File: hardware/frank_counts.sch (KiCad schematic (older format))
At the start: 20 parts, among them U1 MCP23017_SP

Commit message: Wire up all components
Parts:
- added J1: Trigger, symbol Connector:AudioJack2
- added J2: V/OCT, symbol Connector:AudioJack2
- added R?: 7.7k, symbol Device:R
- added R? (x2): 10k, symbol Device:R
- added RV? (x8): R_POT, symbol Device:R_POT
- added SW1: Shift, symbol Switch:SW_Push
- added U?: MCP3008, symbol Analog_ADC:MCP3008
- added U?: MCP4822, symbol Analog_DAC:MCP4822
- added U? (x2): LM324, symbol Amplifier_Operational:LM324
- renumbered A1 to A?, D1 to D?, D2 to D?, D3 to D?, D4 to D?, D5 to D?, D6 to D?, D7 to D?, D8 to D?, R1 to R?, R2 to R?, R3 to R?, R4 to R?, R5 to R?, R6 to R?, R7 to R?, R8 to R?, R9 to R?, R10 to R?, U1 to U?
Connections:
- net labels added: +12V
- wire segments 71 -> 174
- no-connect marks 10 -> 11
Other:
- note added: "Don’t forget power stabilising CAPS!!"
- moved on the sheet: R?

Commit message: Name some resistors
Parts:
- gave numbers to parts that had none: 12
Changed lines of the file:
@@
 Connection ~ 3050 800
 $Comp
-L Device:R R?
+L Device:R R2
 U 1 1 5EB1EFDE
 P 3500 1000
-F 0 "R?" H 3570 1046 50  0000 L CNN
+F 0 "R2" H 3570 1046 50  0000 L CNN
 F 1 "1k" H 3570 955 50  0000 L CNN
 F 2 "" V 3430 1000 50  0001 C CNN
@@
 $EndComp
 $Comp
-L Device:R R?
+L Device:R R3
 U 1 1 5EB24FDB
 P 6600 2200
-F 0 "R?" V 6393 2200 50  0000 C CNN
+F 0 "R3" V 6393 2200 50  0000 C CNN
 F 1 "200" V 6484 2200 50  0000 C CNN
 F 2 "" V 6530 2200 50  0001 C CNN
@@
 $EndComp
 $Comp
-L Device:R R?
+L Device:R R4
 U 1 1 5EB2606A
 P 7150 2200
-F 0 "R?" V 6943 2200 50  0000 C CNN
+F 0 "R4" V 6943 2200 50  0000 C CNN
 F 1 "200" V 7034 2200 50  0000 C CNN
 F 2 "" V 7080 2200 50  0001 C CNN
@@
 $EndComp
 $Comp
-L Device:R R?
+L Device:R R5
 U 1 1 5EB26460
 P 7700 2200
-F 0 "R?" V 7493 2200 50  0000 C CNN
+F 0 "R5" V 7493 2200 50  0000 C CNN
 F 1 "200" V 7584 2200 50  0000 C CNN
 F 2 "" V 7630 2200 50  0001 C CNN
@@
 $EndComp
 $Comp
-L Device:R R?
+L Device:R R6
 U 1 1 5EB268FE
 P 8250 2200
-F 0 "R?" V 8043 2200 50  0000 C CNN
+F 0 "R6" V 8043 2200 50  0000 C CNN
 F 1 "200" V 8134 2200 50  0000 C CNN
 F 2 "" V 8180 2200 50  0001 C CNN
@@
 $EndComp
 $Comp
-L Device:R R?
+L Device:R R7
 U 1 1 5EB26BCE
 P 8800 2200
-F 0 "R?" V 8593 2200 50  0000 C CNN
+F 0 "R7" V 8593 2200 50  0000 C CNN
 F 1 "200" V 8684 2200 50  0000 C CNN
 F 2 "" V 8730 2200 50  0001 C CNN
@@
 $EndComp
 $Comp
-L Device:R R?
+L Device:R R8
 U 1 1 5EB270AB
 P 9350 2200
-F 0 "R?" V 9143 2200 50  0000 C CNN
+F 0 "R8" V 9143 2200 50  0000 C CNN
 F 1 "200" V 9234 2200 50  0000 C CNN
 F 2 "" V 9280 2200 50  0001 C CNN
@@
 $EndComp
 $Comp
-L Device:R R?
+L Device:R R9
 U 1 1 5EB2750A
 P 9900 2200
-F 0 "R?" V 9693 2200 50  0000 C CNN
+F 0 "R9" V 9693 2200 50  0000 C CNN
 F 1 "200" V 9784 2200 50  0000 C CNN
 F 2 "" V 9830 2200 50  0001 C CNN
@@
 $EndComp
 $Comp
-L Device:R R?
+L Device:R R10
 U 1 1 5EB27EEC
 P 10450 2200
-F 0 "R?" V 10243 2200 50  0000 C CNN
+F 0 "R10" V 10243 2200 50  0000 C CNN
 F 1 "200" V 10334 2200 50  0000 C CNN
 F 2 "" V 10380 2200 50  0001 C CNN
@@
 	5300 5450 6800 5450
 $Comp
-L Device:R R?
+L Device:R R12
 U 1 1 5EEC68B4
 P 7150 6250
-F 0 "R?" V 6943 6250 50  0000 C CNN
+F 0 "R12" V 6943 6250 50  0000 C CNN
 F 1 "7.7k" V 7034 6250 50  0000 C CNN
 F 2 "" V 7080 6250 50  0001 C CNN
@@
 	7000 5050 7000 5250
 $Comp
-L Device:R R?
+L Device:R R11
 U 1 1 5EF2D5A3
 P 6200 6250
-F 0 "R?" V 5993 6250 50  0000 C CNN
+F 0 "R11" V 5993 6250 50  0000 C CNN
 F 1 "10k" V 6084 6250 50  0000 C CNN
 F 2 "" V 6130 6250 50  0001 C CNN
@@
 	1250 1650 1300 1650
 $Comp
-L Device:R R?
+L Device:R R1
 U 1 1 5F110ED0
 P 1300 1900
-F 0 "R?" V 1093 1900 50  0000 C CNN
+F 0 "R1" V 1093 1900 50  0000 C CNN
 F 1 "10k" V 1184 1900 50  0000 C CNN
 F 2 "" V 1230 1900 50  0001 C CNN

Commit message: Start v2 of schematic, using STM32
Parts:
- removed A?: Arduino_UNO_R3, Module:Arduino_UNO_R3, symbol MCU_Module:Arduino_UNO_R3
- removed D? (x8): LED, symbol Device:LED
- removed J1: Trigger, symbol Connector:AudioJack2
- removed J2: V/OCT, symbol Connector:AudioJack2
- removed R1, R11: 10k, symbol Device:R
- removed R10, R3, R4, R5, R6, R7, R8, R9: 200, symbol Device:R
- removed R12: 7.7k, symbol Device:R
- removed R2, R?: 1k, symbol Device:R
- removed RV? (x8): R_POT, symbol Device:R_POT
- removed SW1: Shift, symbol Switch:SW_Push
- removed U?: MCP23017_SP, Package_DIP:DIP-28_W7.62mm, symbol Interface_Expansion:MCP23017_SP
- removed U?: MCP3008, symbol Analog_ADC:MCP3008
- removed U?: MCP4822, symbol Analog_DAC:MCP4822
- removed U? (x2): LM324, symbol Amplifier_Operational:LM324
- added U?: STM32F303VCTx, Package_QFP:LQFP-100_14x14mm_P0.5mm, symbol MCU_ST_STM32F3:STM32F303VCTx
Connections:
- net labels removed: +12V, +5V, GND
- wire segments 174 -> 2
- no-connect marks 11 -> 0
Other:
- note removed: "Don’t forget power stabilising CAPS!!"

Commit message: Update schematics
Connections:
- net labels added: DAC_CS, DAC_DATA, DAC_SCK, TRIGGER_IN, TRIGGER_JACK_DETECT
- wire segments 2 -> 11
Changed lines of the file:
@@
 Comment4 ""
 $EndDescr
-$Sheet
-S 7200 1350 950  400
-U 5ED4085B
-F0 "Trigger Input" 50
-F1 "trigger_input.sch" 50
-F2 "JACK_DETECT" O L 7200 1650 50
-F3 "TRIGGER_IN" O L 7200 1450 50
-$EndSheet
 $Comp
 L MCU_ST_STM32F3:STM32F303VCTx U?
@@
 $EndComp
 Wire Wire Line
-	7200 1450 6950 1450
+	8150 1450 6950 1450
 Wire Wire Line
-	7200 1650 6950 1650
+	8150 1650 6950 1650
+Wire Wire Line
+	6950 2050 7150 2050
+Wire Wire Line
+	6950 1750 7950 1750
+Wire Wire Line
+	6950 1850 7550 1850
+Text Label 7250 1450 0    50   ~ 0
+TRIGGER_IN
+Text Label 7050 1650 0    50   ~ 0
+TRIGGER_JACK_DETECT
+Wire Wire Line
+	7150 2050 7150 3300
+Wire Wire Line
+	7150 3300 8600 3300
+Wire Wire Line
+	7550 1850 7550 3150
+Wire Wire Line
+	7550 3150 8600 3150
+Wire Wire Line
+	7950 1750 7950 3000
+Wire Wire Line
+	7950 3000 8600 3000
+Text Label 7950 2400 1    50   ~ 0
+DAC_CS
+Text Label 7550 2550 1    50   ~ 0
+DAC_SCK
+Text Label 7150 2800 1    50   ~ 0
+DAC_DATA
 $Sheet
-S 9050 2300 850  850
+S 8150 1350 950  400
+U 5ED4085B
+F0 "Trigger Input" 50
+F1 "trigger_input.sch" 50
+F2 "JACK_DETECT" O L 8150 1650 50
+F3 "TRIGGER_IN" O L 8150 1450 50
+$EndSheet
+$Sheet
+S 8600 2850 550  600
 U 5ED37B53
 F0 "DAC" 50
 F1 "dac.sch" 50
+F2 "SCK" I L 8600 3150 50
+F3 "MOSI" I L 8600 3300 50
+F4 "CS" I L 8600 3000 50
 $EndSheet
 $EndSCHEMATC

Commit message: Add CV-out schematics
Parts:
- removed U?: STM32F303VCTx, Package_QFP:LQFP-100_14x14mm_P0.5mm, symbol MCU_ST_STM32F3:STM32F303VCTx
- added U?: STM32F302RBT6, Package_QFP:LQFP-64_10x10mm_P0.5mm, symbol MCU_ST_STM32F3:STM32F302RBTx
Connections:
- net labels removed: DAC_CS, DAC_DATA, DAC_SCK, TRIGGER_IN, TRIGGER_JACK_DETECT
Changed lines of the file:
@@
 $Descr A4 11693 8268
 encoding utf-8
-Sheet 1 3
+Sheet 1 4
 Title "frank.counts"
 Date "2020-05-04"
@@
 Comment4 ""
 $EndDescr
-$Comp
-L MCU_ST_STM32F3:STM32F303VCTx U?
-U 1 1 5ED4887B
-P 6150 3750
-F 0 "U?" H 6150 861 50  0000 C CNN
-F 1 "STM32F303VCTx" H 6150 770 50  0000 C CNN
-F 2 "Package_QFP:LQFP-100_14x14mm_P0.5mm" H 5550 1150 50  0001 R CNN
-F 3 "http://www.st.com/st-web-ui/static/active/en/resource/technical/document/datasheet/DM00058181.pdf" H 6150 3750 50  0001 C CNN
-	1    6150 3750
-	1    0    0    -1
-$EndComp
 Wire Wire Line
-	8150 1450 6950 1450
+	9050 1450 7850 1450
 Wire Wire Line
-	8150 1650 6950 1650
+	9050 1650 7850 1650
 Wire Wire Line
-	6950 2050 7150 2050
+	6150 2700 6350 2700
 Wire Wire Line
-	6950 1750 7950 1750
+	6150 2400 7150 2400
 Wire Wire Line
-	6950 1850 7550 1850
-Text Label 7250 1450 0    50   ~ 0
-TRIGGER_IN
-Text Label 7050 1650 0    50   ~ 0
-TRIGGER_JACK_DETECT
+	6150 2500 6750 2500
 Wire Wire Line
-	7150 2050 7150 3300
+	6350 2700 6350 3950
 Wire Wire Line
-	7150 3300 8600 3300
+	6350 3950 7800 3950
 Wire Wire Line
-	7550 1850 7550 3150
+	6750 2500 6750 3800
 Wire Wire Line
-	7550 3150 8600 3150
+	6750 3800 7800 3800
 Wire Wire Line
-	7950 1750 7950 3000
+	7150 2400 7150 3650
 Wire Wire Line
-	7950 3000 8600 3000
-Text Label 7950 2400 1    50   ~ 0
-DAC_CS
-Text Label 7550 2550 1    50   ~ 0
-DAC_SCK
-Text Label 7150 2800 1    50   ~ 0
-DAC_DATA
+	7150 3650 7800 3650
 $Sheet
-S 8150 1350 950  400
+S 9050 1350 950  400
 U 5ED4085B
 F0 "Trigger Input" 50
 F1 "trigger_input.sch" 50
-F2 "JACK_DETECT" O L 8150 1650 50
-F3 "TRIGGER_IN" O L 8150 1450 50
+F2 "JACK_DETECT" O L 9050 1650 50
+F3 "TRIGGER_IN" O L 9050 1450 50
 $EndSheet
 $Sheet
-S 8600 2850 550  600
+S 7800 3500 550  600
 U 5ED37B53
 F0 "DAC" 50
 F1 "dac.sch" 50
-F2 "SCK" I L 8600 3150 50
-F3 "MOSI" I L 8600 3300 50
-F4 "CS" I L 8600 3000 50
+F2 "dac_sck" I L 7800 3800 50
+F3 "dac_cs" I L 7800 3650 50
+F4 "dac_mosi" I L 7800 3950 50
 $EndSheet
+$Comp
+L MCU_ST_STM32F3:STM32F302RBTx U?
+U 1 1 5FBA4493
+P 5450 3600
+F 0 "U?" H 5450 1711 50  0000 C CNN
+F 1 "STM32F302RBT6" H 5450 1620 50  0000 C CNN
+F 2 "Package_QFP:LQFP-64_10x10mm_P0.5mm" H 4850 1900 50  0001 R CNN
+F 3 "http://www.st.com/st-web-ui/static/active/en/resource/technical/document/datasheet/DM00094064.pdf" H 5450 3600 50  0001 C CNN
+	1    5450 3600
+	1    0    0    -1
+$EndComp
 $EndSCHEMATC

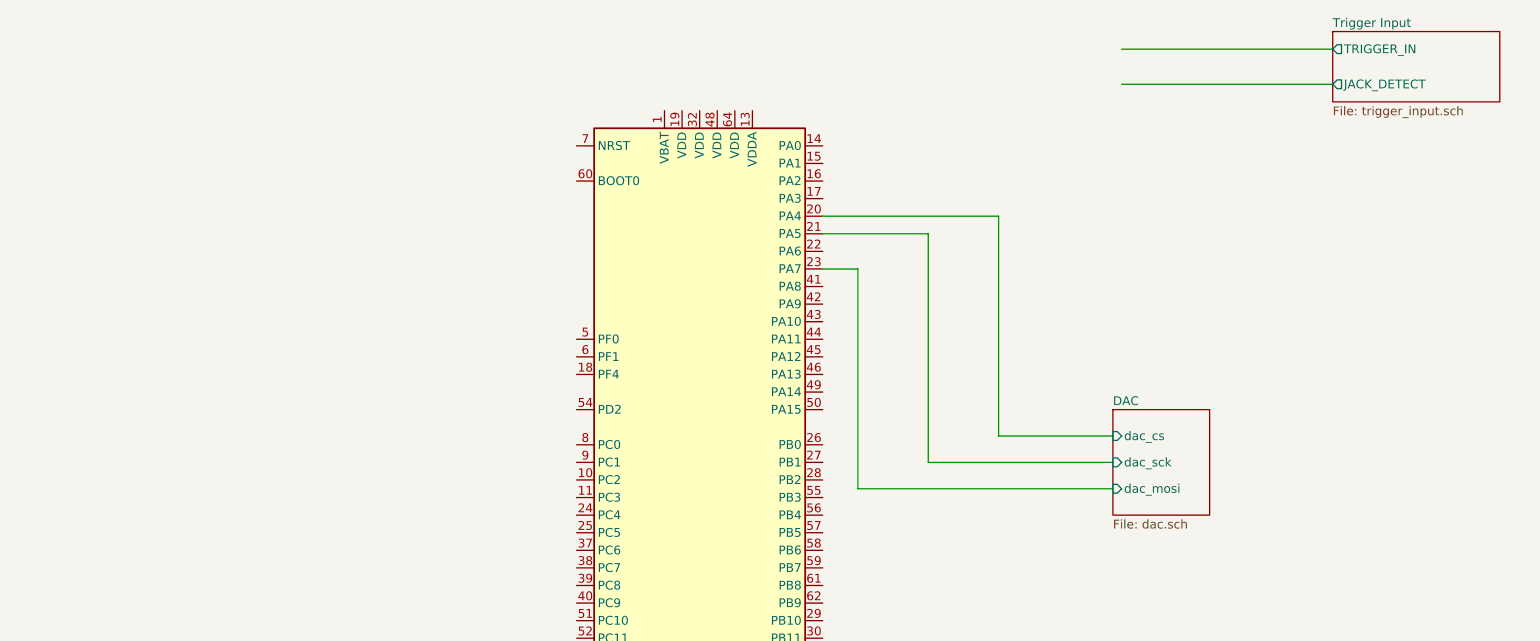
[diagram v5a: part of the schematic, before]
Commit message: Add CV inputs schematics
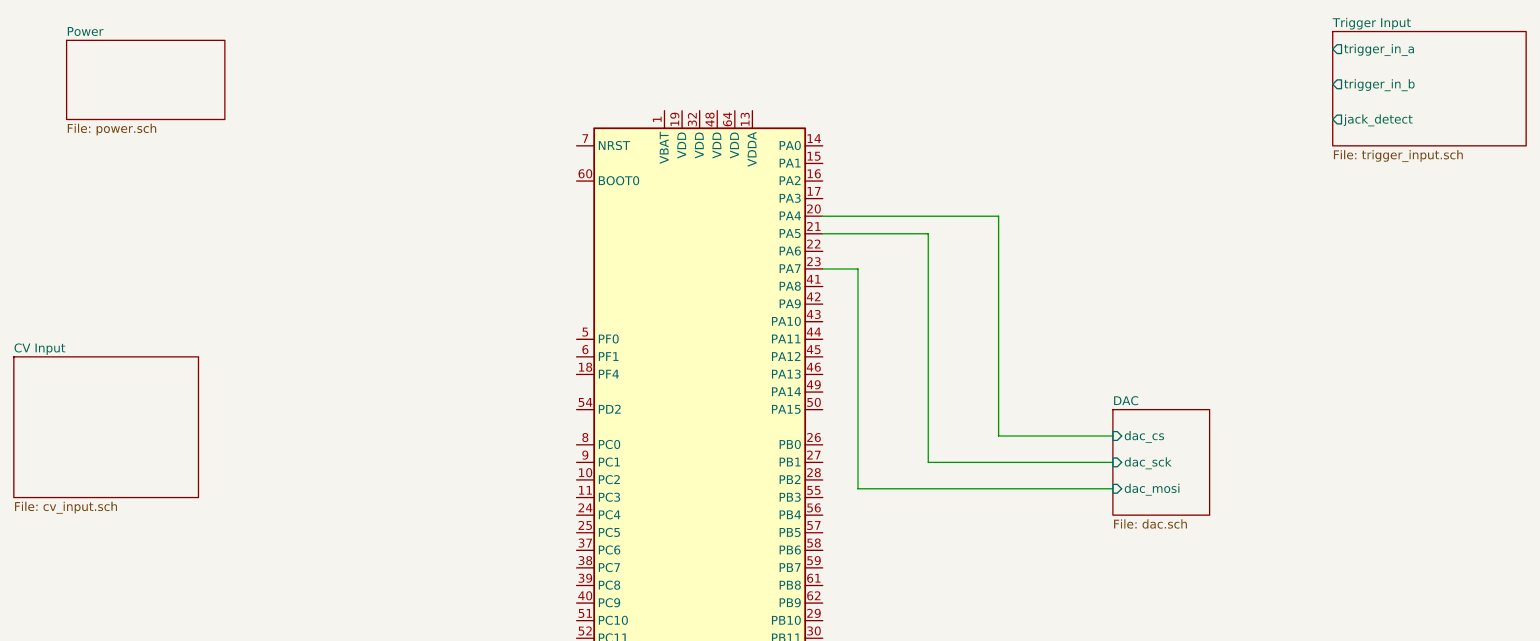
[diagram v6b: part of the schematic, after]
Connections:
- wire segments 11 -> 9
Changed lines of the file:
@@
 $Descr A4 11693 8268
 encoding utf-8
-Sheet 1 4
+Sheet 1 6
 Title "frank.counts"
 Date "2020-05-04"
@@
 Comment4 ""
 $EndDescr
-Wire Wire Line
-	9050 1450 7850 1450
-Wire Wire Line
-	9050 1650 7850 1650
 Wire Wire Line
 	6150 2700 6350 2700
@@
 	7150 3650 7800 3650
 $Sheet
-S 9050 1350 950  400
+S 9050 1350 1100 650
 U 5ED4085B
 F0 "Trigger Input" 50
 F1 "trigger_input.sch" 50
-F2 "JACK_DETECT" O L 9050 1650 50
-F3 "TRIGGER_IN" O L 9050 1450 50
+F2 "jack_detect" O L 9050 1850 50
+F3 "trigger_in_a" O L 9050 1450 50
+F4 "trigger_in_b" O L 9050 1650 50
 $EndSheet
 $Sheet
@@
 	1    0    0    -1
 $EndComp
+$Sheet
+S 1550 3200 1050 800
+U 5FCA3E21
+F0 "CV Input" 50
+F1 "cv_input.sch" 50
+$EndSheet
+$Sheet
+S 1850 1400 900  450
+U 5FCB1CD7
+F0 "Power" 50
+F1 "power.sch" 50
+$EndSheet
 $EndSCHEMATC
